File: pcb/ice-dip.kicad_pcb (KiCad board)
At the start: 4 copper layers, 17.8 x 50.8 mm, 40 parts, among them J1 Pin1-20, J2 Pin21-40, U1 ICE40UP5K-SG48ITR50, U2 W25Q16JVSNIQ, U3 LDL1117S33R, U4 MCP1700T-1202E/TT, U5 SN74CBTD3861PWR, U6 SN74CBTD3861PWR, U7 SN74CBTD3861PWR, U8 SN74CBTD3861PWR, X1 SG-5032CAN

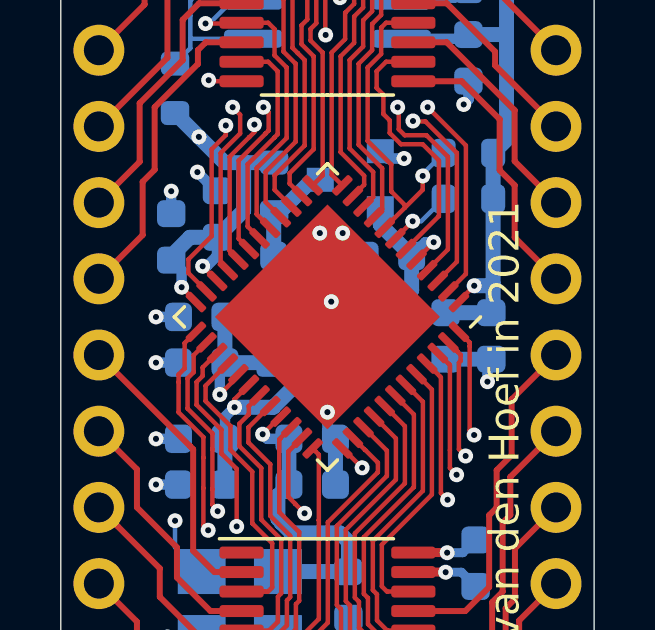
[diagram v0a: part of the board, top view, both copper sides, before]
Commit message: Library for ICE-DIP component. Fixing some small issues.
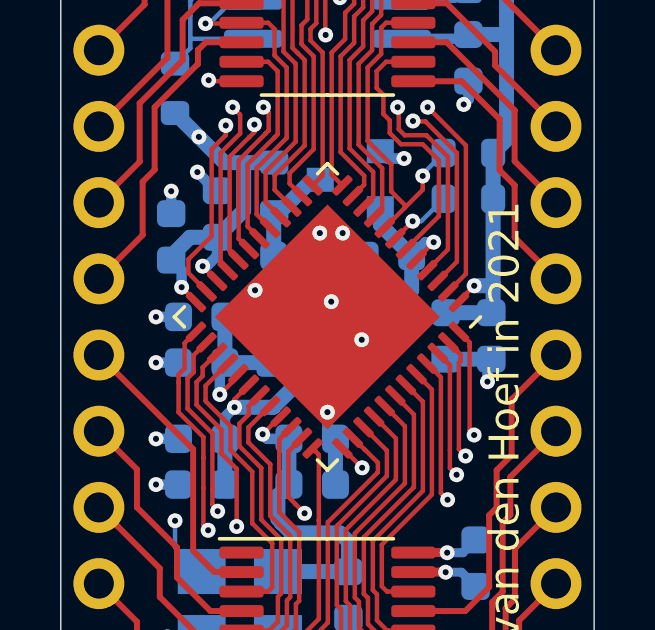
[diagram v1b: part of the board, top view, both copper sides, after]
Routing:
- net GND: vias 30 -> 32
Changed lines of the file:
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@@
     (thickness 1.6)
     (drawings 7)
-    (tracks 1040)
+    (tracks 1042)
     (zones 0)
     (modules 40)
@@
     (add_net "Net-(R3-Pad2)")
     (add_net "Net-(R4-Pad2)")
-    (add_net "Net-(U5-Pad2)")
-    (add_net "Net-(X1-Pad1)")
     (add_net P1)
     (add_net P10)
@@
   (gr_line (start 133.35 123.19) (end 133.35 72.39) (layer Edge.Cuts) (width 0.05))
   (gr_line (start 115.57 123.19) (end 133.35 123.19) (layer Edge.Cuts) (width 0.05))
+  (via (at 125.603 98.552) (size 0.5) (drill 0.2) (layers F.Cu B.Cu) (net 1))
+  (via (at 122.047 96.901) (size 0.5) (drill 0.2) (layers F.Cu B.Cu) (net 1))
   (via (at 124.968 94.996) (size 0.5) (drill 0.2) (layers F.Cu B.Cu) (net 1))
   (via (at 124.46 100.965) (size 0.5) (drill 0.2) (layers F.Cu B.Cu) (net 1))

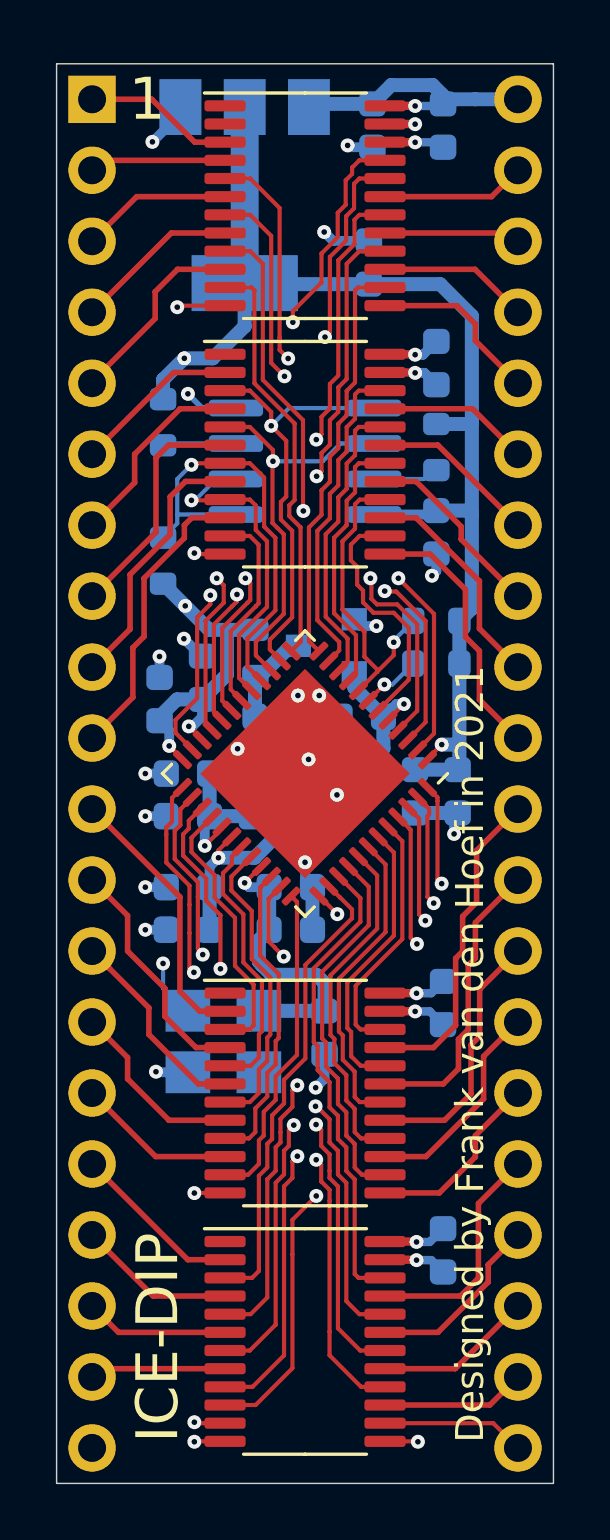
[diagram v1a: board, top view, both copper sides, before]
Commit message: Added extra copper pours. Added gerbers + bill of materials.
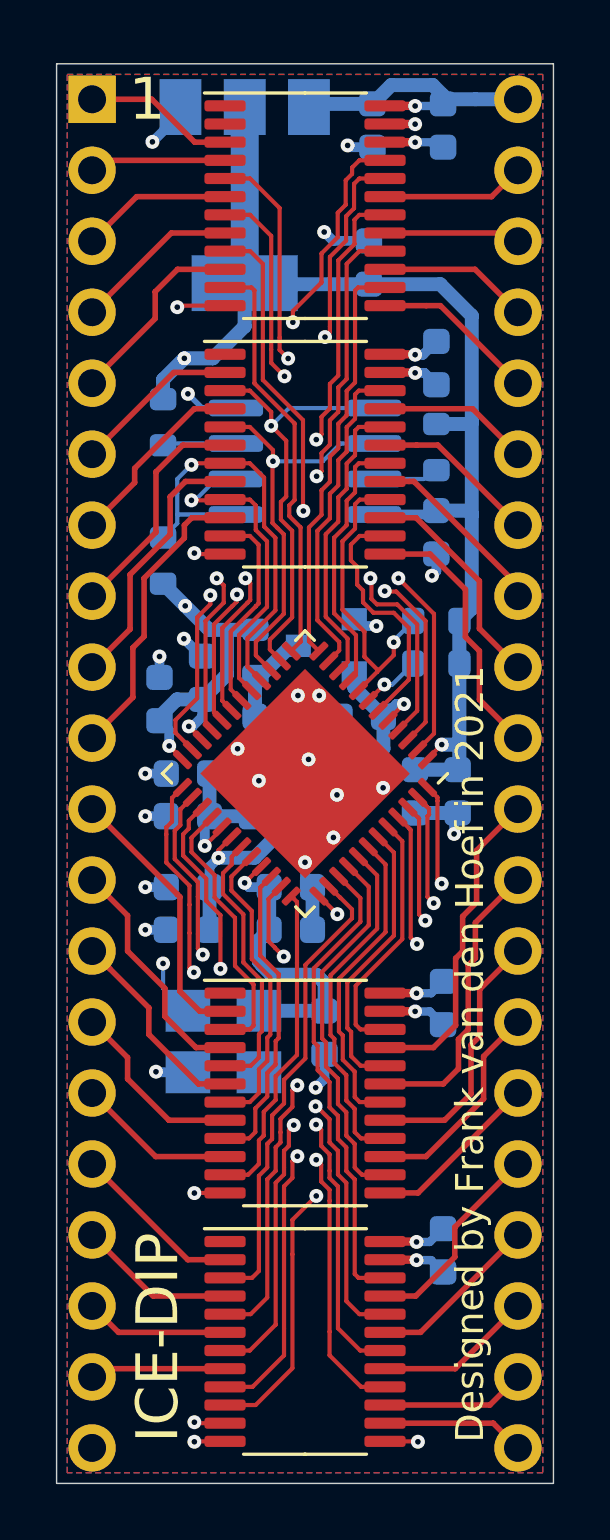
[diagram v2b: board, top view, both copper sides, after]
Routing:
- net P25: track 8.28 -> 7.34 mm
- net GND: vias 32 -> 35
- added copper zone on B.Cu, net GND
- added copper zone on F.Cu, net GND
